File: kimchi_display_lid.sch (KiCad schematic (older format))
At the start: 8 parts, among them J1 DF40HC(3.5)-60DS, J2 DF40HC(3.5)-60DS, U1 24C32

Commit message: Add board outline
Signed-off-by: Michael Welling <mwelling@ieee.org>
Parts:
- added H5, H6, H7, H8: MountingHole_Pad, kimchi_ulid:MountingHole_3mm_Pad, symbol Mechanical:MountingHole_Pad
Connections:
- net GND: now also H5.1, H6.1, H7.1, H8.1
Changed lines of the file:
@@
 EESchema Schematic File Version 4
-LIBS:kimchi_ulid-cache
+LIBS:kimchi_display_lid-cache
 EELAYER 26 0
 EELAYER END
@@
 	1    0    0    -1
 $EndComp
+$Comp
+L Mechanical:MountingHole_Pad H5
+U 1 1 5FD7395F
+P 14250 2200
+F 0 "H5" H 14350 2249 50  0000 L CNN
+F 1 "MountingHole_Pad" H 14350 2158 50  0000 L CNN
+F 2 "kimchi_ulid:MountingHole_3mm_Pad" H 14350 2112 50  0001 L CNN
+F 3 "~" H 14250 2200 50  0001 C CNN
+	1    14250 2200
+	1    0    0    -1
+$EndComp
+$Comp
+L Mechanical:MountingHole_Pad H6
+U 1 1 5FD73966
+P 14250 2700
+F 0 "H6" H 14350 2749 50  0000 L CNN
+F 1 "MountingHole_Pad" H 14350 2658 50  0000 L CNN
+F 2 "kimchi_ulid:MountingHole_3mm_Pad" H 14250 2700 50  0001 C CNN
+F 3 "~" H 14250 2700 50  0001 C CNN
+	1    14250 2700
+	1    0    0    -1
+$EndComp
+$Comp
+L Mechanical:MountingHole_Pad H7
+U 1 1 5FD7396D
+P 15350 2200
+F 0 "H7" H 15450 2249 50  0000 L CNN
+F 1 "MountingHole_Pad" H 15450 2158 50  0000 L CNN
+F 2 "kimchi_ulid:MountingHole_3mm_Pad" H 15350 2200 50  0001 C CNN
+F 3 "~" H 15350 2200 50  0001 C CNN
+	1    15350 2200
+	1    0    0    -1
+$EndComp
+$Comp
+L Mechanical:MountingHole_Pad H8
+U 1 1 5FD73974
+P 15350 2700
+F 0 "H8" H 15450 2749 50  0000 L CNN
+F 1 "MountingHole_Pad" H 15450 2658 50  0000 L CNN
+F 2 "kimchi_ulid:MountingHole_3mm_Pad" H 15350 2700 50  0001 C CNN
+F 3 "~" H 15350 2700 50  0001 C CNN
+	1    15350 2700
+	1    0    0    -1
+$EndComp
+$Comp
+L power:GND #PWR01
+U 1 1 5FD7397B
+P 14250 2300
+F 0 "#PWR01" H 14250 2050 50  0001 C CNN
+F 1 "GND" H 14255 2127 50  0000 C CNN
+F 2 "" H 14250 2300 50  0001 C CNN
+F 3 "" H 14250 2300 50  0001 C CNN
+	1    14250 2300
+	1    0    0    -1
+$EndComp
+$Comp
+L power:GND #PWR02
+U 1 1 5FD73981
+P 14250 2800
+F 0 "#PWR02" H 14250 2550 50  0001 C CNN
+F 1 "GND" H 14255 2627 50  0000 C CNN
+F 2 "" H 14250 2800 50  0001 C CNN
+F 3 "" H 14250 2800 50  0001 C CNN
+	1    14250 2800
+	1    0    0    -1
+$EndComp
+$Comp
+L power:GND #PWR03
+U 1 1 5FD73987
+P 15350 2300
+F 0 "#PWR03" H 15350 2050 50  0001 C CNN
+F 1 "GND" H 15355 2127 50  0000 C CNN
+F 2 "" H 15350 2300 50  0001 C CNN
+F 3 "" H 15350 2300 50  0001 C CNN
+	1    15350 2300
+	1    0    0    -1
+$EndComp
+$Comp
+L power:GND #PWR04
+U 1 1 5FD7398D
+P 15350 2800
+F 0 "#PWR04" H 15350 2550 50  0001 C CNN
+F 1 "GND" H 15355 2627 50  0000 C CNN
+F 2 "" H 15350 2800 50  0001 C CNN
+F 3 "" H 15350 2800 50  0001 C CNN
+	1    15350 2800
+	1    0    0    -1
+$EndComp

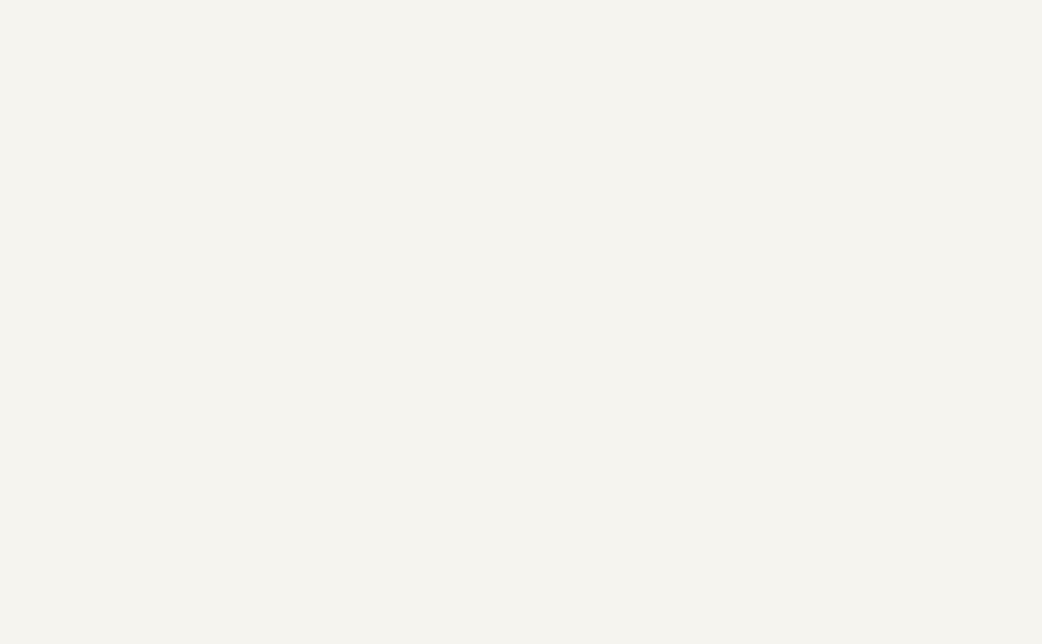
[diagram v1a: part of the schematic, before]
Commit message: Add LCD backlight LED driver
Signed-off-by: Michael Welling <mwelling@ieee.org>
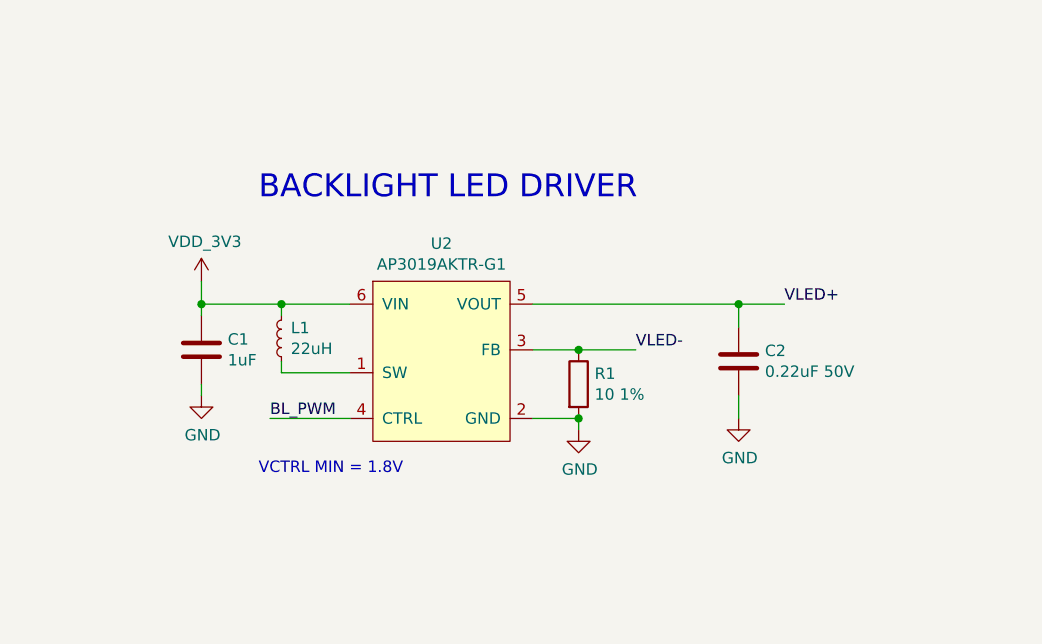
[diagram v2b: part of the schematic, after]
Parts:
- added C1: 1uF, Capacitor_SMD:C_0603_1608Metric, symbol Device:C
- added C2: 0.22uF 50V, Capacitor_SMD:C_0603_1608Metric, symbol Device:C
- added L1: 22uH, Inductor_SMD:L_Taiyo-Yuden_MD-1616, symbol Device:L_Small
- added R1: 10 1%, Resistor_SMD:R_0603_1608Metric, symbol Device:R
- added U2: AP3019AKTR-G1, Package_TO_SOT_SMD:SOT-23-6, symbol kimchi_ulid:AP3019AKTR-G1
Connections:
- net GND: now also C1.2, C2.2, R1.2, U2.2 (GND)
- net VDD_3V3: now also C1.1, L1.2, U2.6 (VIN)
- new net: L1.1, U2.1 (SW)
- new net BL_PWM: U2.4 (CTRL)
- new net VLED+: C2.1, U2.5 (VOUT)
- new net VLED-: R1.1, U2.3 (FB)
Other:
- note added: "BACKLIGHT LED DRIVER"
- note added: "VCTRL MIN = 1.8V"
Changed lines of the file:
@@
 	1    0    0    -1
 $EndComp
+$Comp
+L kimchi_ulid:AP3019AKTR-G1 U2
+U 1 1 5FD73956
+P 7000 6100
+F 0 "U2" H 7000 6465 50  0000 C CNN
+F 1 "AP3019AKTR-G1" H 7000 6374 50  0000 C CNN
+F 2 "Package_TO_SOT_SMD:SOT-23-6" H 6800 6100 50  0001 C CNN
+F 3 "" H 6800 6100 50  0001 C CNN
+	1    7000 6100
+	1    0    0    -1
+$EndComp
+$Comp
+L Device:L_Small L1
+U 1 1 5FD73CA2
+P 6300 6150
+F 0 "L1" H 6259 6104 50  0000 R CNN
+F 1 "22uH" H 6259 6195 50  0000 R CNN
+F 2 "Inductor_SMD:L_Taiyo-Yuden_MD-1616" H 6300 6150 50  0001 C CNN
+F 3 "~" H 6300 6150 50  0001 C CNN
+	1    6300 6150
+	-1   0    0    1
+$EndComp
+Wire Wire Line
+	6600 6300 6300 6300
+Wire Wire Line
+	6300 6300 6300 6250
+Wire Wire Line
+	6600 6000 6300 6000
+Wire Wire Line
+	6300 6050 6300 6000
+Connection ~ 6300 6000
+Wire Wire Line
+	6300 6000 5950 6000
+$Comp
+L Device:R R1
+U 1 1 5FD77C84
+P 7600 6350
+F 0 "R1" H 7670 6396 50  0000 L CNN
+F 1 "10 1%" H 7670 6305 50  0000 L CNN
+F 2 "Resistor_SMD:R_0603_1608Metric" V 7530 6350 50  0001 C CNN
+F 3 "~" H 7600 6350 50  0001 C CNN
+	1    7600 6350
+	1    0    0    -1
+$EndComp
+Wire Wire Line
+	7400 6500 7600 6500
+Wire Wire Line
+	7400 6200 7600 6200
+$Comp
+L power:GND #PWR0114
+U 1 1 5FD7A3F5
+P 7600 6550
+F 0 "#PWR0114" H 7600 6300 50  0001 C CNN
+F 1 "GND" H 7605 6377 50  0000 C CNN
+F 2 "" H 7600 6550 50  0001 C CNN
+F 3 "" H 7600 6550 50  0001 C CNN
+	1    7600 6550
+	1    0    0    -1
+$EndComp
+Wire Wire Line
+	7600 6500 7600 6550
+Connection ~ 7600 6500
+Wire Wire Line
+	7600 6200 7850 6200
+Connection ~ 7600 6200
+Text Label 7850 6200 0    50   ~ 0
+VLED-
+Wire Wire Line
+	7400 6000 8300 6000
+Text Label 8500 6000 0    50   ~ 0
+VLED+
+$Comp
+L Device:C C1
+U 1 1 5FD7E377
+P 5950 6200
+F 0 "C1" H 6065 6246 50  0000 L CNN
+F 1 "1uF" H 6065 6155 50  0000 L CNN
+F 2 "Capacitor_SMD:C_0603_1608Metric" H 5988 6050 50  0001 C CNN
+F 3 "~" H 5950 6200 50  0001 C CNN
+	1    5950 6200
+	1    0    0    -1
+$EndComp
+$Comp
+L power:GND #PWR0115
+U 1 1 5FD7E423
+P 5950 6400
+F 0 "#PWR0115" H 5950 6150 50  0001 C CNN
+F 1 "GND" H 5955 6227 50  0000 C CNN
+F 2 "" H 5950 6400 50  0001 C CNN
+F 3 "" H 5950 6400 50  0001 C CNN
+	1    5950 6400
+	1    0    0    -1
+$EndComp
+Wire Wire Line
+	5950 6350 5950 6400
+Wire Wire Line
+	5950 6050 5950 6000
+Connection ~ 5950 6000
+$Comp
+L Device:C C2
+U 1 1 5FD85741
+P 8300 6250
+F 0 "C2" H 8415 6296 50  0000 L CNN
+F 1 "0.22uF 50V" H 8415 6205 50  0000 L CNN
+F 2 "Capacitor_SMD:C_0603_1608Metric" H 8338 6100 50  0001 C CNN
+F 3 "~" H 8300 6250 50  0001 C CNN
+	1    8300 6250
+	1    0    0    -1
+$EndComp
+$Comp
+L power:GND #PWR0116
+U 1 1 5FD86FB6
+P 8300 6500
+F 0 "#PWR0116" H 8300 6250 50  0001 C CNN
+F 1 "GND" H 8305 6327 50  0000 C CNN
+F 2 "" H 8300 6500 50  0001 C CNN
+F 3 "" H 8300 6500 50  0001 C CNN
+	1    8300 6500
+	1    0    0    -1
+$EndComp
+Wire Wire Line
+	8300 6400 8300 6500
+Wire Wire Line
+	8300 6100 8300 6000
+Connection ~ 8300 6000
+Wire Wire Line
+	8300 6000 8500 6000
+Text Notes 6200 5550 0    100  ~ 0
+BACKLIGHT LED DRIVER
+$Comp
+L kimchi_ulid:VDD_3V3 #PWR0117
+U 1 1 5FD8A47B
+P 5950 5900
+F 0 "#PWR0117" H 5950 5750 50  0001 C CNN
+F 1 "VDD_3V3" H 5965 6073 50  0000 C CNN
+F 2 "" H 5950 5900 50  0001 C CNN
+F 3 "" H 5950 5900 50  0001 C CNN
+	1    5950 5900
+	1    0    0    -1
+$EndComp
+Wire Wire Line
+	5950 5900 5950 6000
+Wire Wire Line
+	6600 6500 6250 6500
+Text Label 6250 6500 0    50   ~ 0
+BL_PWM
+Text Notes 6200 6750 0    50   ~ 0
+VCTRL MIN = 1.8V
 $EndSCHEMATC

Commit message: Bump inductor to a big package
Signed-off-by: Michael Welling <mwelling@ieee.org>
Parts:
- L1: footprint Inductor_SMD:L_Taiyo-Yuden_MD-1616 -> Inductor_SMD:L_Taiyo-Yuden_MD-4040
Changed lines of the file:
@@
 F 0 "L1" H 6259 6104 50  0000 R CNN
 F 1 "22uH" H 6259 6195 50  0000 R CNN
-F 2 "Inductor_SMD:L_Taiyo-Yuden_MD-1616" H 6300 6150 50  0001 C CNN
+F 2 "Inductor_SMD:L_Taiyo-Yuden_MD-4040" H 6300 6150 50  0001 C CNN
 F 3 "~" H 6300 6150 50  0001 C CNN
 	1    6300 6150

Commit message: Add some manufacturer part numbers
So I don't forget them. ;)

Signed-off-by: Michael Welling <mwelling@ieee.org>
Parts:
- J1, J2: Part (none) -> DF40HC(3.5)-60DS
- L1: Part (none) -> TYA4012220M-10
- U2: Part (none) -> AP3019AKTR-G1
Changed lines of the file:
@@
 F 2 "kimchi_ulid:DF40HC(3.5)-60DS" H 9650 2650 50  0001 C CNN
 F 3 "~" H 9650 2650 50  0001 C CNN
+F 4 "DF40HC(3.5)-60DS" H 0   0   50  0001 C CNN "Part"
 	1    9650 2650
 	1    0    0    -1
@@
 F 2 "kimchi_ulid:DF40HC(3.5)-60DS" H 7050 2650 50  0001 C CNN
 F 3 "~" H 7050 2650 50  0001 C CNN
+F 4 "DF40HC(3.5)-60DS" H 0   0   50  0001 C CNN "Part"
 	1    7050 2650
 	1    0    0    -1
@@
 F 2 "Package_TO_SOT_SMD:SOT-23-6" H 6800 6100 50  0001 C CNN
 F 3 "" H 6800 6100 50  0001 C CNN
+F 4 "AP3019AKTR-G1" H 0   0   50  0001 C CNN "Part"
 	1    7000 6100
 	1    0    0    -1
@@
 F 2 "Inductor_SMD:L_Taiyo-Yuden_MD-4040" H 6300 6150 50  0001 C CNN
 F 3 "~" H 6300 6150 50  0001 C CNN
+F 4 "TYA4012220M-10" H 0   0   50  0001 C CNN "Part"
 	1    6300 6150
 	-1   0    0    1
